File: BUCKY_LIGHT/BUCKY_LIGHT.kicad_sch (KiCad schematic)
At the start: 116 parts, among them Q1 Q_Photo_NPN, Q10 Q_Photo_NPN, Q11 Q_Photo_NPN, Q12 Q_Photo_NPN, Q13 Q_Photo_NPN, Q14 Q_Photo_NPN, Q15 Q_Photo_NPN, Q16 Q_Photo_NPN, Q17 Q_Photo_NPN, Q18 Q_Photo_NPN, Q19 Q_Photo_NPN, Q2 Q_Photo_NPN, Q20 Q_Photo_NPN, Q21 Q_Photo_NPN, Q22 Q_Photo_NPN, Q23 Q_Photo_NPN, Q24 Q_Photo_NPN, Q25 Q_Photo_NPN, Q26 Q_Photo_NPN, Q27 Q_Photo_NPN, Q28 Q_Photo_NPN, Q3 Q_Photo_NPN, Q4 Q_Photo_NPN, Q5 Q_Photo_NPN, Q6 Q_Photo_NPN, Q7 Q_Photo_NPN, Q8 Q_Photo_NPN, Q9 Q_Photo_NPN, U1 FRONT, U2 RIGHT, U3 DOWN, U4 LEFT

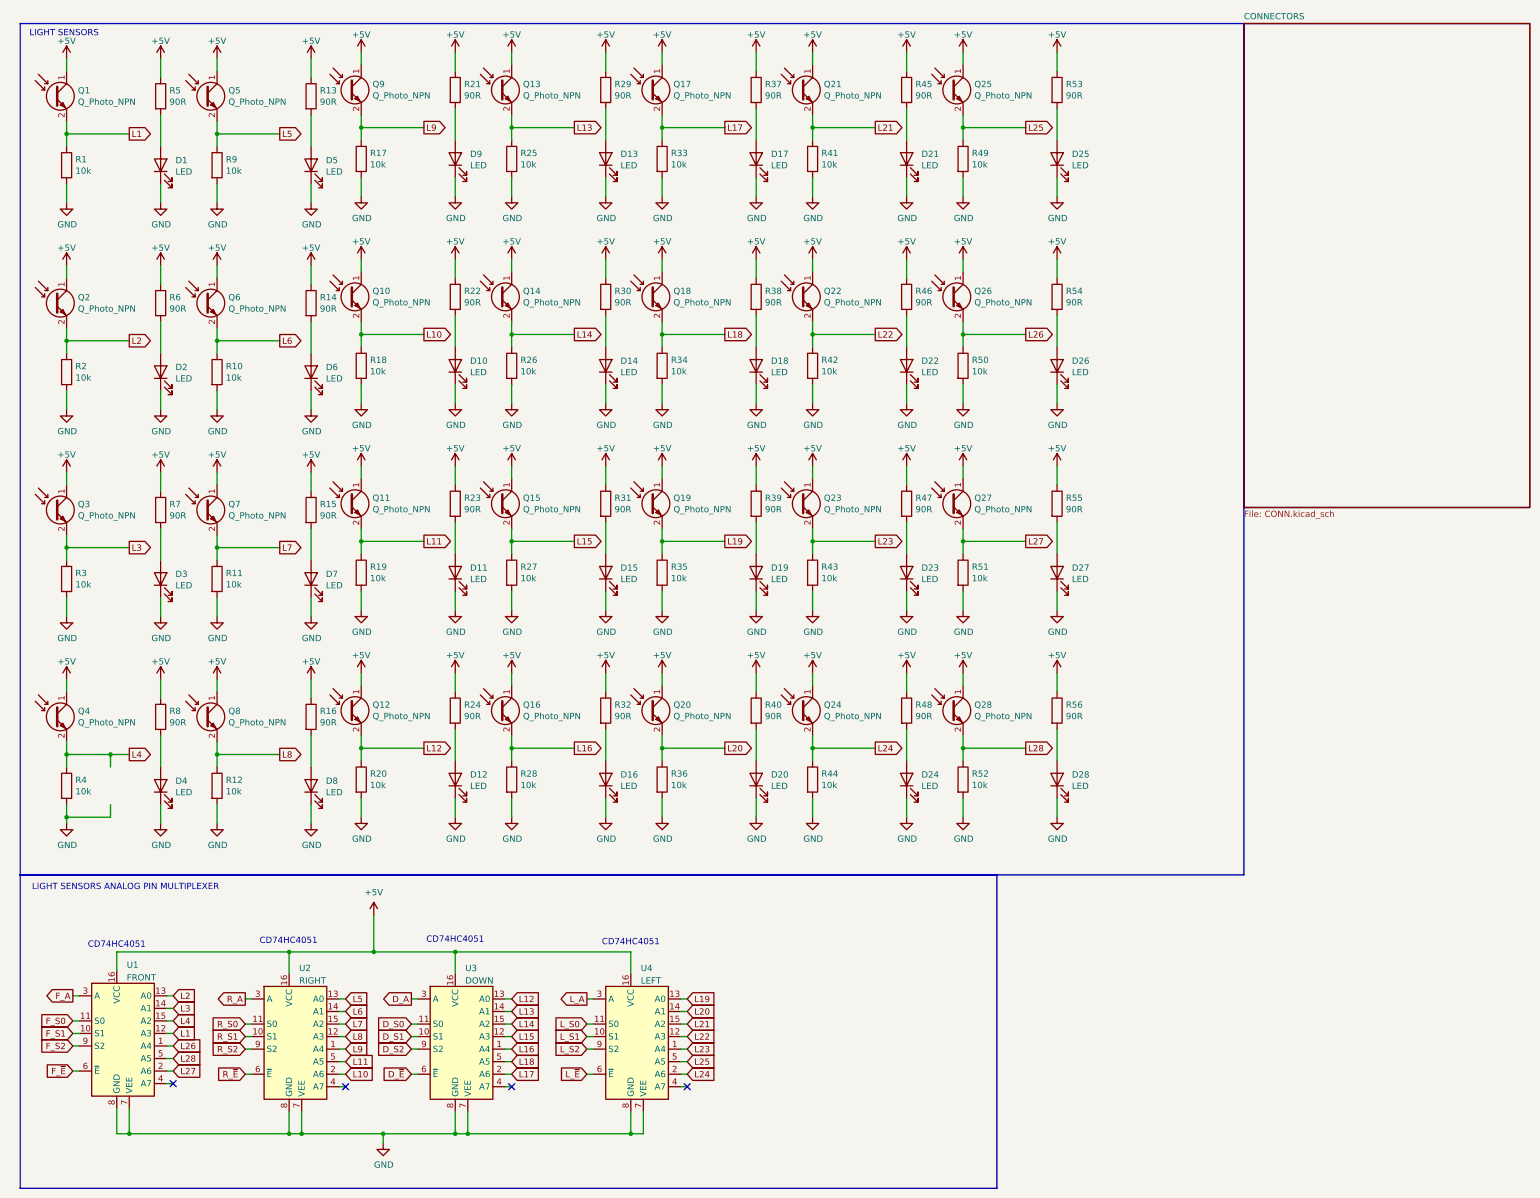
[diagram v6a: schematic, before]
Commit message: chore: start on ldr instead of Q_Photo_N, interrupt instead of analog multiplexer. And a signal for front,back,left,right
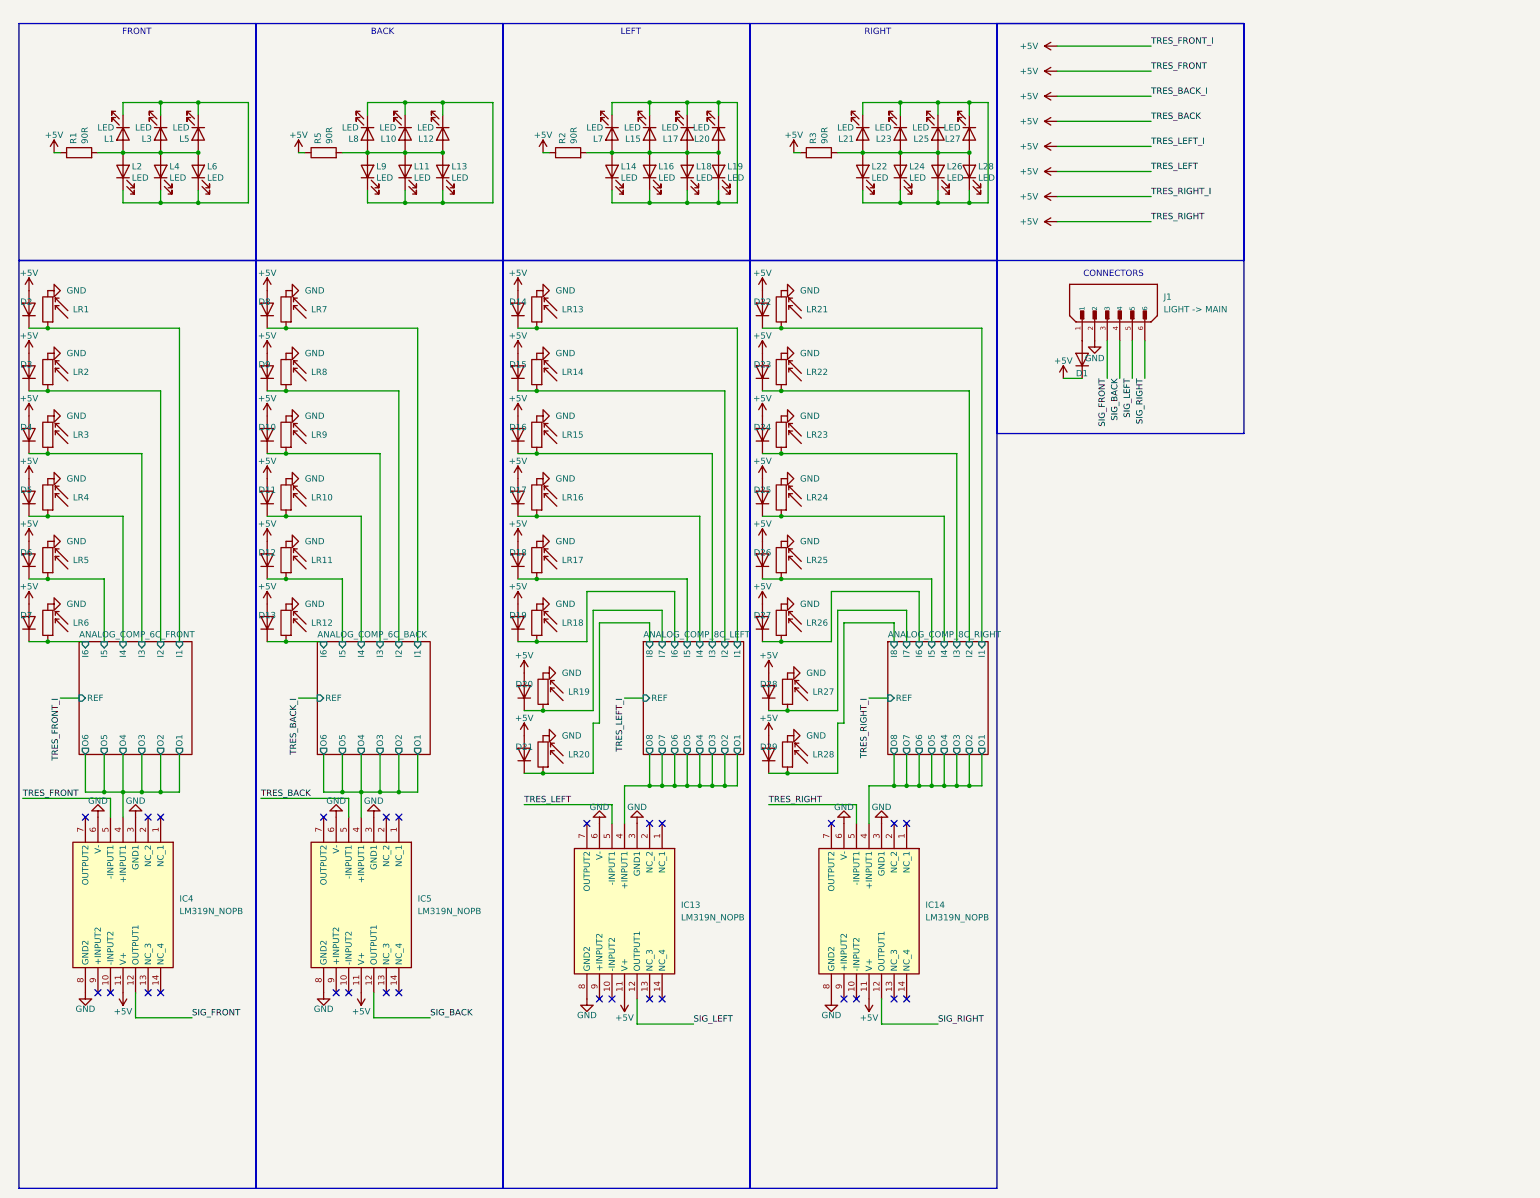
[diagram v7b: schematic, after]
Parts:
- removed D1, D10, D11, D12, D13, D14, D15, D16, D17, D18, D19, D2, D20, D21, D22, D23, D24, D25, D26, D27, D28, D3, D4, D5, D6, D7, D8, D9: LED, LED_SMD:LED_PLCC-2, symbol Device:LED
- removed Q1, Q10, Q11, Q12, Q13, Q14, Q15, Q16, Q17, Q18, Q19, Q2, Q20, Q21, Q22, Q23, Q24, Q25, Q26, Q27, Q28, Q3, Q4, Q5, Q6, Q7, Q8, Q9: Q_Photo_NPN, BUCKY_LIGHT:XDCR_ALS-PT19-315C_L177_TR8, symbol Device:Q_Photo_NPN
- removed R10, R11, R12, R17, R18, R19, R20, R25, R26, R27, R28, R33, R34, R35, R36, R4, R41, R42, R43, R44, R49, R50, R51, R52, R9: 10k, Resistor_SMD:R_0603_1608Metric, symbol Device:R
- removed R13, R14, R15, R16, R21, R22, R23, R24, R29, R30, R31, R32, R37, R38, R39, R40, R45, R46, R47, R48, R53, R54, R55, R56, R6, R7, R8: 90R, Resistor_SMD:R_0603_1608Metric, symbol Device:R
- removed U1: FRONT, Package_SO:SOIC-16_3.9x9.9mm_P1.27mm, symbol 74xx:74HC4051
- removed U2: RIGHT, Package_SO:SOIC-16_3.9x9.9mm_P1.27mm, symbol 74xx:74HC4051
- removed U3: DOWN, Package_SO:SOIC-16_3.9x9.9mm_P1.27mm, symbol 74xx:74HC4051
- removed U4: LEFT, Package_SO:SOIC-16_3.9x9.9mm_P1.27mm, symbol 74xx:74HC4051
- added D1, D10, D11, D12, D13, D14, D15, D16, D17, D18, D19, D2, D20, D21, D22, D23, D24, D25, D26, D27, D28, D29, D3, D4, D5, D6, D7, D8, D9: D, symbol Device:D
- added IC13, IC14, IC4, IC5: LM319N_NOPB, DIP794W56P254L1905H533Q14N, symbol ANALOG_COMP:LM319N_NOPB
- added J1: LIGHT -> MAIN, B6B-XH-A:JST_B6B-XH-A, symbol LIGHT_CONN:B6B-XH-A
- added L1, L10, L11, L12, L13, L14, L15, L16, L17, L18, L19, L2, L20, L21, L22, L23, L24, L25, L26, L27, L28, L3, L4, L5, L6, L7, L8, L9: LED, LED_SMD:LED_PLCC-2, symbol Device:LED
- added LR1, LR10, LR11, LR12, LR13, LR14, LR15, LR16, LR17, LR18, LR19, LR2, LR20, LR21, LR22, LR23, LR24, LR25, LR26, LR27, LR28, LR3, LR4, LR5, LR6, LR7, LR8, LR9: R_Photo, symbol Device:R_Photo
- R1, R2, R3: value 10k -> 90R
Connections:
- net L1 is gone; now on net +5V: R1.1
- net L2 is gone; now on net +5V: R2.1
- net L3 is gone; now on net +5V: R3.1
- net +5V: now also D1.1 (K), D10.2 (A), D11.2 (A), D12.2 (A), D13.2 (A), D14.2 (A), D15.2 (A), D16.2 (A), D17.2 (A), D18.2 (A), D19.2 (A), D2.2 (A), D20.2 (A), D21.2 (A), D22.2 (A), D23.2 (A), D24.2 (A), D25.2 (A), D26.2 (A), D27.2 (A), D28.2 (A), D29.2 (A), D3.2 (A), D4.2 (A), D5.2 (A), D6.2 (A), D7.2 (A), D8.2 (A), D9.2 (A), IC13.11 (V+), IC13.5 (-INPUT1), IC14.11 (V+), IC14.5 (-INPUT1), IC4.11 (V+), IC4.5 (-INPUT1), IC5.11 (V+), IC5.5 (-INPUT1)
- net GND: now also IC13.3 (GND1), IC13.6 (V-), IC13.8 (GND2), IC14.3 (GND1), IC14.6 (V-), IC14.8 (GND2), IC4.3 (GND1), IC4.6 (V-), IC4.8 (GND2), IC5.3 (GND1), IC5.6 (V-), IC5.8 (GND2), J1.2, LR1.2, LR10.2, LR11.2, LR12.2, LR13.2, LR14.2, LR15.2, LR16.2, LR17.2, LR18.2, LR19.2, LR2.2, LR20.2, LR21.2, LR22.2, LR23.2, LR24.2, LR25.2, LR26.2, LR27.2, LR28.2, LR3.2, LR4.2, LR5.2, LR6.2, LR7.2, LR8.2, LR9.2; no longer R1.2, R2.2, R3.2
- net at R5.2: now also L10.2 (A), L11.2 (A), L12.2 (A), L13.2 (A), L8.2 (A), L9.2 (A)
- new net: L1.1 (K), L2.1 (K), L3.1 (K), L4.1 (K), L5.1 (K), L6.1 (K)
- new net: L1.2 (A), L2.2 (A), L3.2 (A), L4.2 (A), L5.2 (A), L6.2 (A), R1.2
- new net: L14.2 (A), L15.2 (A), L16.2 (A), L17.2 (A), L18.2 (A), L19.2 (A), L20.2 (A), L7.2 (A), R2.2
- new net: L21.1 (K), L22.1 (K), L23.1 (K), L24.1 (K), L25.1 (K), L26.1 (K), L27.1 (K), L28.1 (K)
- new net: L21.2 (A), L22.2 (A), L23.2 (A), L24.2 (A), L25.2 (A), L26.2 (A), L27.2 (A), L28.2 (A), R3.2
- new net: L14.1 (K), L15.1 (K), L16.1 (K), L17.1 (K), L18.1 (K), L19.1 (K), L20.1 (K), L7.1 (K)
- new net: D1.2 (A), J1.1
- new net: L10.1 (K), L11.1 (K), L12.1 (K), L13.1 (K), L8.1 (K), L9.1 (K)
- new net ANALOG_COMP_6C_BACK/I1: D8.1 (K), LR7.1
- new net ANALOG_COMP_6C_BACK/I2: D9.1 (K), LR8.1
- new net ANALOG_COMP_6C_BACK/I3: D10.1 (K), LR9.1
- new net ANALOG_COMP_6C_BACK/I4: D11.1 (K), LR10.1
- new net ANALOG_COMP_6C_BACK/I5: D12.1 (K), LR11.1
- new net ANALOG_COMP_6C_BACK/I6: D13.1 (K), LR12.1
- new net ANALOG_COMP_6C_BACK/O1: IC5.4 (+INPUT1)
- new net ANALOG_COMP_6C_FRONT/I1: D2.1 (K), LR1.1
- new net ANALOG_COMP_6C_FRONT/I2: D3.1 (K), LR2.1
- new net ANALOG_COMP_6C_FRONT/I3: D4.1 (K), LR3.1
- new net ANALOG_COMP_6C_FRONT/I4: D5.1 (K), LR4.1
- new net ANALOG_COMP_6C_FRONT/I5: D6.1 (K), LR5.1
- new net ANALOG_COMP_6C_FRONT/I6: D7.1 (K), LR6.1
- new net ANALOG_COMP_6C_FRONT/O1: IC4.4 (+INPUT1)
- new net ANALOG_COMP_8C_LEFT/I1: D14.1 (K), LR13.1
- new net ANALOG_COMP_8C_LEFT/I2: D15.1 (K), LR14.1
- new net ANALOG_COMP_8C_LEFT/I3: D16.1 (K), LR15.1
- new net ANALOG_COMP_8C_LEFT/I4: D17.1 (K), LR16.1
- new net ANALOG_COMP_8C_LEFT/I5: D18.1 (K), LR17.1
- new net ANALOG_COMP_8C_LEFT/I6: D19.1 (K), LR18.1
- new net ANALOG_COMP_8C_LEFT/I7: D20.1 (K), LR19.1
- new net ANALOG_COMP_8C_LEFT/I8: D21.1 (K), LR20.1
- new net ANALOG_COMP_8C_LEFT/O1: IC13.4 (+INPUT1)
- new net ANALOG_COMP_8C_RIGHT/I1: D22.1 (K), LR21.1
- new net ANALOG_COMP_8C_RIGHT/I2: D23.1 (K), LR22.1
- new net ANALOG_COMP_8C_RIGHT/I3: D24.1 (K), LR23.1
- new net ANALOG_COMP_8C_RIGHT/I4: D25.1 (K), LR24.1
- new net ANALOG_COMP_8C_RIGHT/I5: D26.1 (K), LR25.1
- new net ANALOG_COMP_8C_RIGHT/I6: D27.1 (K), LR26.1
- new net ANALOG_COMP_8C_RIGHT/I7: D28.1 (K), LR27.1
- new net ANALOG_COMP_8C_RIGHT/I8: D29.1 (K), LR28.1
- new net ANALOG_COMP_8C_RIGHT/O1: IC14.4 (+INPUT1)
- new net SIG_BACK: IC5.12 (OUTPUT1), J1.4
- new net SIG_FRONT: IC4.12 (OUTPUT1), J1.3
- new net SIG_LEFT: IC13.12 (OUTPUT1), J1.5
- new net SIG_RIGHT: IC14.12 (OUTPUT1), J1.6
- no-connect marks 4 -> 28
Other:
- removed sheet CONNECTORS
- added sheet ANALOG_COMP_6C_BACK (ANALOG_COMPARATOR_6_CHANNELS.kicad_sch)
- added sheet ANALOG_COMP_6C_FRONT (ANALOG_COMPARATOR_6_CHANNELS.kicad_sch)
- added sheet ANALOG_COMP_8C_LEFT (ANALOG_COMPARATOR_8_CHANNELS.kicad_sch)
- added sheet ANALOG_COMP_8C_RIGHT (ANALOG_COMPARATOR_8_CHANNELS.kicad_sch)
- note added: "BACK"
- note added: "CONNECTORS"
- note added: "FRONT"
- note added: "LEFT"
- note added: "RIGHT"
- note removed: "CD74HC4051"
- note removed: "LIGHT SENSORS"
- note removed: "LIGHT SENSORS ANALOG PIN MULTIPLEXER"

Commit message: finish up robot (i think)
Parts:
- removed D10, D11, D12, D13, D14, D15, D16, D17, D18, D19, D2, D20, D21, D22, D23, D24, D25, D26, D27, D28, D29, D3, D4, D5, D6, D7, D8, D9: D, symbol Device:D
- removed IC13, IC14, IC4, IC5: LM319N_NOPB, DIP794W56P254L1905H533Q14N, symbol ANALOG_COMP:LM319N_NOPB
- removed L20, L27: LED, LED_SMD:LED_PLCC-2, symbol Device:LED
- removed LR1, LR10, LR11, LR12, LR13, LR14, LR15, LR16, LR17, LR18, LR19, LR2, LR20, LR21, LR22, LR23, LR24, LR25, LR26, LR27, LR28, LR3, LR4, LR5, LR6, LR7, LR8, LR9: R_Photo, symbol Device:R_Photo
- added L14, L7: LED, LED_SMD:LED_PLCC-2_3.4x3.0mm_AK, symbol Device:LED
- added Q1, Q10, Q11, Q12, Q13, Q14, Q15, Q16, Q17, Q18, Q19, Q2, Q20, Q21, Q22, Q23, Q24, Q25, Q26, Q27, Q28, Q3, Q4, Q5, Q6, Q7, Q8, Q9: Q_Photo_NPN, BUCKY_LIGHT:XDCR_ALS-PT19-315C_L177_TR8, symbol Device:Q_Photo_NPN
- added R10, R11, R12, R13, R14, R15, R16, R17, R18, R19, R20, R21, R22, R23, R24, R25, R26, R27, R28, R29, R30, R31, R32, R4, R6, R7, R8, R9: 10k, Resistor_SMD:R_0603_1608Metric, symbol Device:R
- added R33, R35, R37, R39: 20k, Resistor_SMD:R_0603_1608Metric, symbol Device:R
- added REF1, REF2, REF3, REF4: 3362P-1-103, BUCKY_LIGHT:VAR_RESISTOR, symbol VAR_RESISTOR:3362P-1-103
- D1: footprint (none) -> LED_SMD:LED_PLCC-2_3.4x3.0mm_AK
- J1: footprint B6B-XH-A:JST_B6B-XH-A -> BUCKY_LIGHT:LIGHT_CONN
- L1, L10, L11, L12, L13, L2, L28, L3, L4, L5, L6, L8, L9: footprint LED_SMD:LED_PLCC-2 -> LED_SMD:LED_PLCC-2_3.4x3.0mm_AK
- L15: renamed from L7; footprint LED_SMD:LED_PLCC-2 -> LED_SMD:LED_PLCC-2_3.4x3.0mm_AK
- L16: renamed from L14; footprint LED_SMD:LED_PLCC-2 -> LED_SMD:LED_PLCC-2_3.4x3.0mm_AK
- L17: renamed from L15; footprint LED_SMD:LED_PLCC-2 -> LED_SMD:LED_PLCC-2_3.4x3.0mm_AK
- L18: renamed from L16; footprint LED_SMD:LED_PLCC-2 -> LED_SMD:LED_PLCC-2_3.4x3.0mm_AK
- L19: renamed from L17; footprint LED_SMD:LED_PLCC-2 -> LED_SMD:LED_PLCC-2_3.4x3.0mm_AK
- L20: renamed from L18; footprint LED_SMD:LED_PLCC-2 -> LED_SMD:LED_PLCC-2_3.4x3.0mm_AK
- L21: renamed from L19; footprint LED_SMD:LED_PLCC-2 -> LED_SMD:LED_PLCC-2_3.4x3.0mm_AK
- L22: renamed from L21; footprint LED_SMD:LED_PLCC-2 -> LED_SMD:LED_PLCC-2_3.4x3.0mm_AK
- L23: renamed from L22; footprint LED_SMD:LED_PLCC-2 -> LED_SMD:LED_PLCC-2_3.4x3.0mm_AK
- L24: renamed from L23; footprint LED_SMD:LED_PLCC-2 -> LED_SMD:LED_PLCC-2_3.4x3.0mm_AK
- L25: renamed from L24; footprint LED_SMD:LED_PLCC-2 -> LED_SMD:LED_PLCC-2_3.4x3.0mm_AK
- L26: renamed from L25; footprint LED_SMD:LED_PLCC-2 -> LED_SMD:LED_PLCC-2_3.4x3.0mm_AK
- L27: renamed from L26; footprint LED_SMD:LED_PLCC-2 -> LED_SMD:LED_PLCC-2_3.4x3.0mm_AK
- R1, R2, R3, R5: value 90R -> 10k
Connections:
- net +5V: now also Q1.1 (C), Q10.1 (C), Q11.1 (C), Q12.1 (C), Q13.1 (C), Q14.1 (C), Q15.1 (C), Q16.1 (C), Q17.1 (C), Q18.1 (C), Q19.1 (C), Q2.1 (C), Q20.1 (C), Q21.1 (C), Q22.1 (C), Q23.1 (C), Q24.1 (C), Q25.1 (C), Q26.1 (C), Q27.1 (C), Q28.1 (C), Q3.1 (C), Q4.1 (C), Q5.1 (C), Q6.1 (C), Q7.1 (C), Q8.1 (C), Q9.1 (C), R29.1, R30.1, R31.1, R32.1, R33.1, R35.1, R37.1, R39.1; no longer R1.1, R2.1, R3.1, R5.1
- net GND: now also L1.1 (K), L10.1 (K), L11.1 (K), L12.1 (K), L13.1 (K), L15.1 (K), L16.1 (K), L17.1 (K), L18.1 (K), L19.1 (K), L2.1 (K), L20.1 (K), L21.1 (K), L22.1 (K), L23.1 (K), L24.1 (K), L25.1 (K), L26.1 (K), L27.1 (K), L28.1 (K), L3.1 (K), L4.1 (K), L5.1 (K), L6.1 (K), L8.1 (K), L9.1 (K), R1.2, R2.2, R3.2, R5.2, L14.1 (K), L7.1 (K), R10.2, R11.2, R12.2, R13.2, R14.2, R15.2, R16.2, R17.2, R18.2, R19.2, R20.2, R21.2, R22.2, R23.2, R24.2, R25.2, R26.2, R27.2, R28.2, R4.2, R6.2, R7.2, R8.2, R9.2, REF1.2 (WIPER), REF1.3 (CW), REF2.2 (WIPER), REF2.3 (CW), REF3.2 (WIPER), REF3.3 (CW), REF4.2 (WIPER), REF4.3 (CW)
- net at L1.2 (A), L2.2 (A), L3.2 (A)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: now also L7.2 (A), R29.2; no longer R1.2
- net at L15.2 (A), L16.2 (A), L17.2 (A)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: now also R31.2; no longer R2.2
- net at L22.2 (A), L23.2 (A), L24.2 (A)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: now also R32.2; no longer R3.2
- net at L10.2 (A), L11.2 (A), L12.2 (A)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: now also L14.2 (A), R30.2; no longer R5.2
- new net ANALOG_COMP_BACK/I1: Q15.2 (E), R15.1
- new net ANALOG_COMP_BACK/I2: Q16.2 (E), R16.1
- new net ANALOG_COMP_BACK/I3: Q17.2 (E), R17.1
- new net ANALOG_COMP_BACK/I4: Q18.2 (E), R18.1
- new net ANALOG_COMP_BACK/I5: Q19.2 (E), R19.1
- new net ANALOG_COMP_BACK/I6: Q20.2 (E), R20.1
- new net ANALOG_COMP_BACK/I7: Q21.2 (E), R21.1
- new net ANALOG_COMP_FRONT/I1: Q1.2 (E), R1.1
- new net ANALOG_COMP_FRONT/I2: Q2.2 (E), R2.1
- new net ANALOG_COMP_FRONT/I3: Q3.2 (E), R3.1
- new net ANALOG_COMP_FRONT/I4: Q4.2 (E), R4.1
- new net ANALOG_COMP_FRONT/I5: Q5.2 (E), R5.1
- new net ANALOG_COMP_FRONT/I6: Q6.2 (E), R6.1
- new net ANALOG_COMP_FRONT/I7: Q7.2 (E), R7.1
- new net ANALOG_COMP_LEFT/I1: Q22.2 (E), R22.1
- new net ANALOG_COMP_LEFT/I2: Q23.2 (E), R23.1
- new net ANALOG_COMP_LEFT/I3: Q24.2 (E), R24.1
- new net ANALOG_COMP_LEFT/I4: Q25.2 (E), R25.1
- new net ANALOG_COMP_LEFT/I5: Q26.2 (E), R26.1
- new net ANALOG_COMP_LEFT/I6: Q27.2 (E), R27.1
- new net ANALOG_COMP_LEFT/I7: Q28.2 (E), R28.1
- new net ANALOG_COMP_RIGHT/I1: Q8.2 (E), R8.1
- new net ANALOG_COMP_RIGHT/I2: Q9.2 (E), R9.1
- new net ANALOG_COMP_RIGHT/I3: Q10.2 (E), R10.1
- new net ANALOG_COMP_RIGHT/I4: Q11.2 (E), R11.1
- new net ANALOG_COMP_RIGHT/I5: Q12.2 (E), R12.1
- new net ANALOG_COMP_RIGHT/I6: Q13.2 (E), R13.1
- new net ANALOG_COMP_RIGHT/I7: Q14.2 (E), R14.1
- new net TRES_BACK_I: R35.2, REF2.1 (CCW)
- new net TRES_FRONT_I: R33.2, REF1.1 (CCW)
- new net TRES_LEFT_I: R37.2, REF3.1 (CCW)
- new net TRES_RIGHT_I: R39.2, REF4.1 (CCW)
- no-connect marks 28 -> 0
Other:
- removed sheet ANALOG_COMP_6C_BACK
- removed sheet ANALOG_COMP_6C_FRONT
- removed sheet ANALOG_COMP_8C_LEFT
- removed sheet ANALOG_COMP_8C_RIGHT
- added sheet ANALOG_COMP_BACK (ANALOG_COMPARATOR_8_CHANNELS.kicad_sch)
- added sheet ANALOG_COMP_FRONT (ANALOG_COMPARATOR_8_CHANNELS.kicad_sch)
- added sheet ANALOG_COMP_LEFT (ANALOG_COMPARATOR_8_CHANNELS.kicad_sch)
- added sheet ANALOG_COMP_RIGHT (ANALOG_COMPARATOR_8_CHANNELS.kicad_sch)
- moved on the sheet: D1, J1
